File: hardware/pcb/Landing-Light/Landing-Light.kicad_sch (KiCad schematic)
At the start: 26 parts, among them J1 Conn_01x04, SW1 SW_SPST, SW2 SW_SP3T, U1 BQ25172DSGR, U2 TPS61022

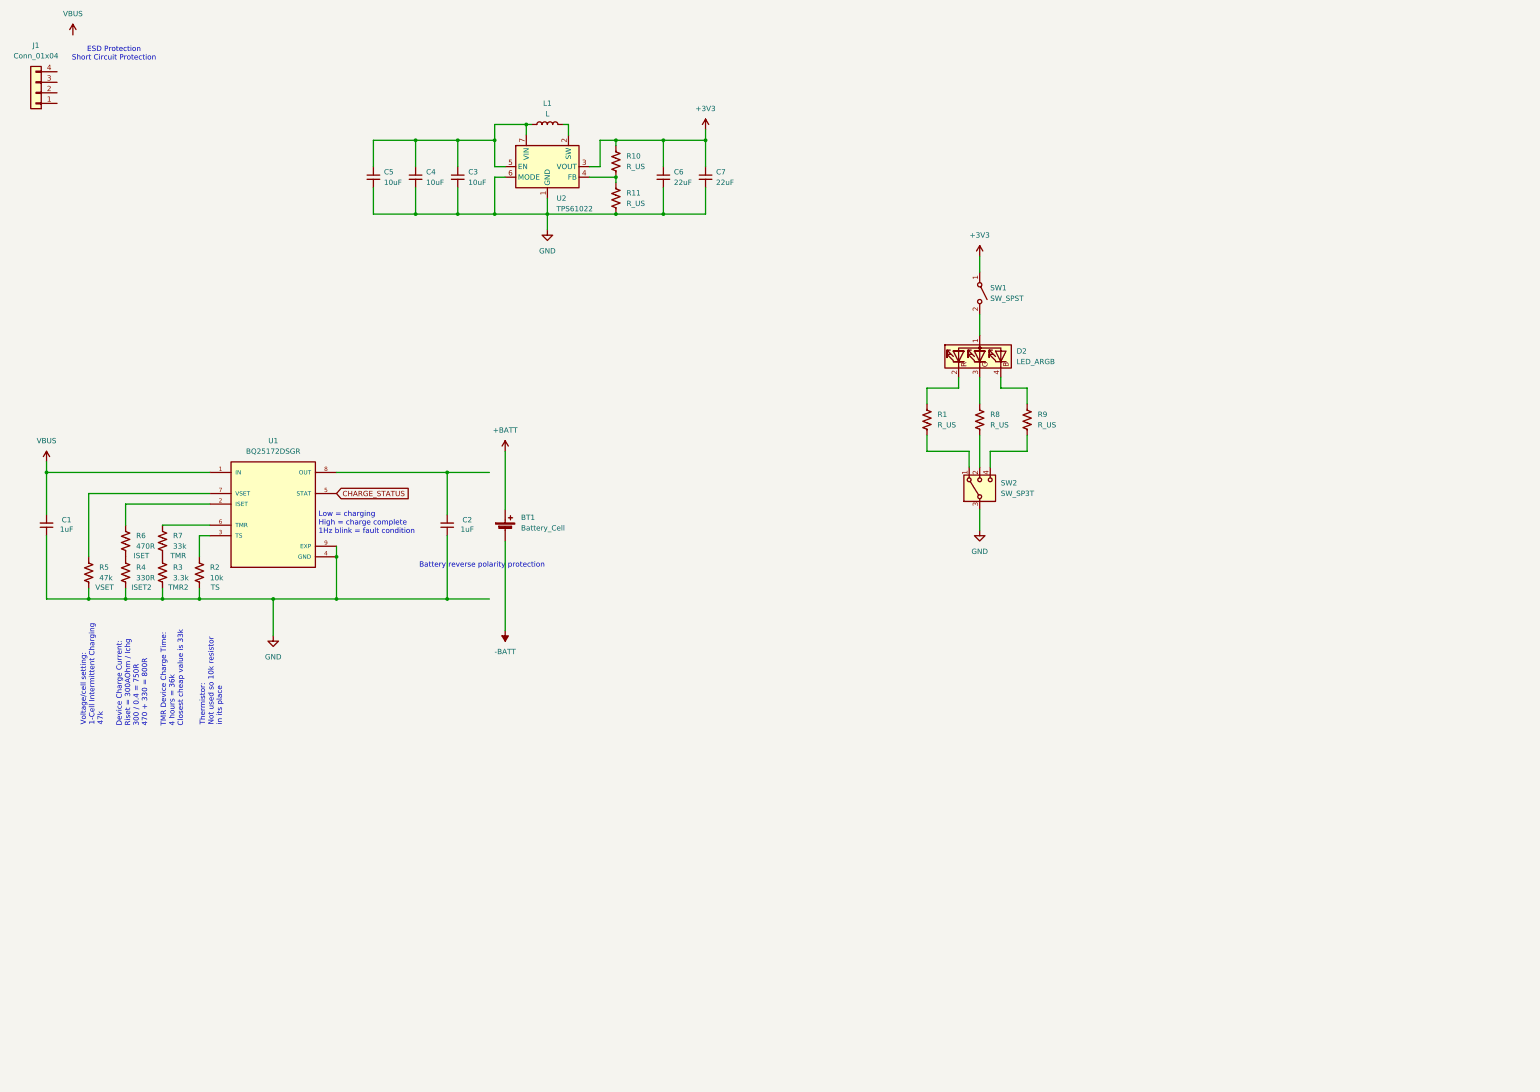
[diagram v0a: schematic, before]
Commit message: Footprints complete
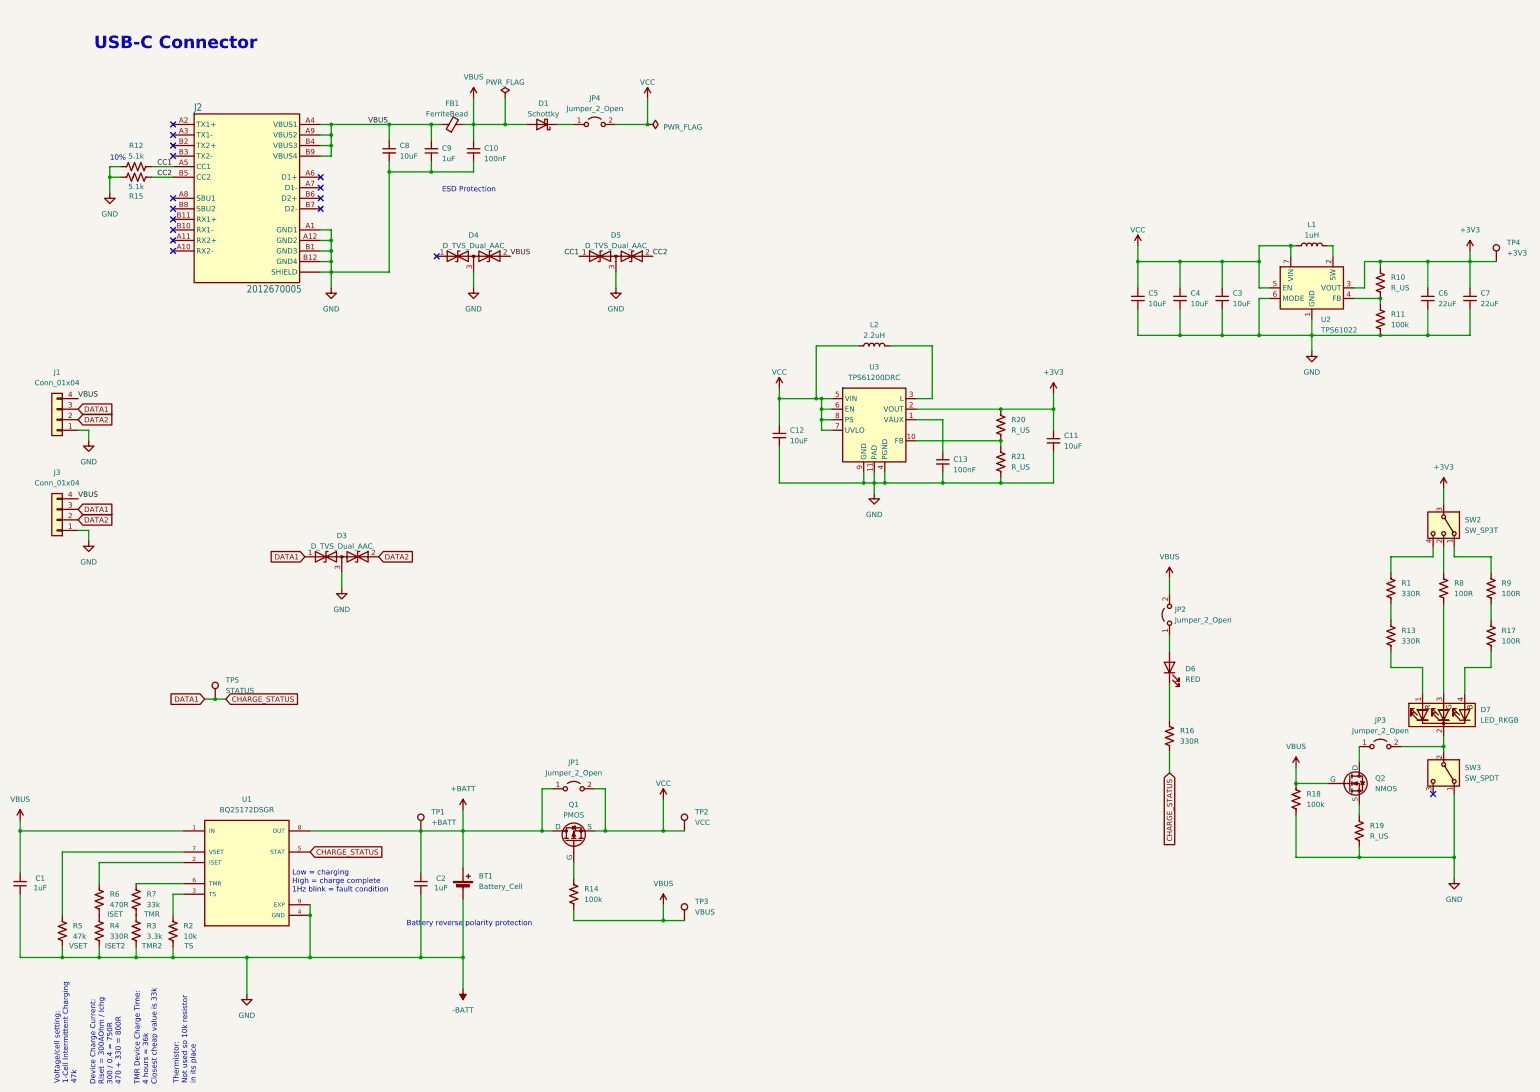
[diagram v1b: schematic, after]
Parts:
- removed D2: LED_ARGB, LED_THT:LED_D5.0mm-4_RGB_Staggered_Pins, symbol Device:LED_ARGB
- removed SW1: SW_SPST, Button_Switch_SMD:SW_SPDT_PCM12, symbol Switch:SW_SPST
- added C10, C13: 100nF, Capacitor_SMD:C_0402_1005Metric, symbol Device:C_Small
- added C11, C12, C8: 10uF, Capacitor_SMD:C_0603_1608Metric, symbol Device:C_Small
- added C9: 1uF, Capacitor_SMD:C_0402_1005Metric, symbol Device:C_Small
- added D1: Schottky, Diode_SMD:D_SMA, symbol Device:D_Schottky
- added D3, D4, D5: D_TVS_Dual_AAC, Package_TO_SOT_SMD:SOT-23, symbol Device:D_TVS_Dual_AAC
- added D6: RED, LED_SMD:LED_0805_2012Metric, symbol Device:LED
- added D7: LED_RKGB, LED_THT:LED_D5.0mm-4_RGB, symbol Device:LED_RKGB
- added FB1: FerriteBead, Diode_SMD:D_0805_2012Metric, symbol Device:FerriteBead_Small
- added J2: 2012670005, Landing-Light:MOLEX_2012670005, symbol ESP32_Dev_Board-eagle-import:2012670005
- added J3: Conn_01x04, Connector_PinHeader_2.54mm:PinHeader_1x04_P2.54mm_Vertical, symbol Connector_Generic:Conn_01x04
- added JP1, JP2, JP3, JP4: Jumper_2_Open, Jumper:SolderJumper-2_P1.3mm_Open_Pad1.0x1.5mm, symbol Jumper:Jumper_2_Open
- added L2: 2.2uH, Inductor_SMD:L_Sunlord_SWPA3015S, symbol Device:L
- added Q1: PMOS, Package_TO_SOT_SMD:SOT-23, symbol Simulation_SPICE:PMOS
- added Q2: NMOS, Package_TO_SOT_SMD:SOT-23-3, symbol Simulation_SPICE:NMOS
- added R12, R15: 5.1k, Resistor_SMD:R_0603_1608Metric, symbol Device:R_US
- added R13, R16: 330R, Resistor_SMD:R_0402_1005Metric, symbol Device:R_US
- added R14, R18: 100k, Resistor_SMD:R_0603_1608Metric, symbol Device:R_US
- added R17: 100R, Resistor_SMD:R_0402_1005Metric, symbol Device:R_US
- added R19, R20, R21: R_US, Resistor_SMD:R_0603_1608Metric, symbol Device:R_US
- added SW3: SW_SPDT, Landing-Light:SSSS810201, symbol Switch:SW_SPDT
- added TP1: +BATT, TestPoint:TestPoint_Pad_D1.0mm, symbol Connector:TestPoint
- added TP2: VCC, TestPoint:TestPoint_Pad_D1.0mm, symbol Connector:TestPoint
- added TP3: VBUS, TestPoint:TestPoint_Pad_D1.0mm, symbol Connector:TestPoint
- added TP4: +3V3, TestPoint:TestPoint_Pad_D1.0mm, symbol Connector:TestPoint
- added TP5: STATUS, TestPoint:TestPoint_Pad_D1.0mm, symbol Connector:TestPoint
- added U3: TPS61200DRC, Package_SON:Texas_S-PVSON-N10_ThermalVias, symbol Regulator_Switching:TPS61200DRC
- J1: footprint (none) -> Landing-Light:70AAJ-4-F1G
- L1: value L -> 1uH
- R1: value R_US -> 330R; LCSC (none) -> C25104
- R11: value R_US -> 100k; footprint Resistor_SMD:R_0402_1005Metric -> Resistor_SMD:R_0603_1608Metric; LCSC (none) -> C25803
- R2, R3, R4, R5, R6, R7: footprint Capacitor_SMD:C_0402_1005Metric -> Resistor_SMD:R_0402_1005Metric
- R8, R9: value R_US -> 100R; LCSC (none) -> C25076
- SW2: footprint Button_Switch_SMD:SW_SPDT_PCM12 -> Landing-Light:SSSS812201; LCSC (none) -> C160878; now left out of the parts list
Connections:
- net +3V3: now also SW2.3, C11.1, R20.1, TP4.1, U3.2 (VOUT)
- net +BATT: now also C2.2, U1.8 (OUT), JP1.1 (A), Q1.3 (D), TP1.1
- net -BATT: now also C1.1, C2.1, C3.2, C4.2, C5.2, C6.2, C7.2, J1.1 (Pin_1), R11.2, R2.2, R3.2, R4.2, R5.2, U1.4 (GND), U1.9 (EXP), U2.1 (GND), U2.6 (MODE), C10.2, C11.2, C12.2, C13.2, C8.2, C9.1, D3.3 (common), D4.3 (common), D5.3 (common), J2.A1 (GND1), J2.A12 (GND2), J2.B1 (GND3), J2.B12 (GND4), J2.S1 (SHIELD), J2.S2 (SHIELD), J2.S3 (SHIELD), J2.S4 (SHIELD), J3.1 (Pin_1), R12.1, R15.2, R18.2, R19.2, R21.2, SW3.1 (A), U3.11 (PAD), U3.4 (PGND), U3.9 (GND)
- net CHARGE_STATUS: now also J1.3 (Pin_3), D3.1 (A1), J3.3 (Pin_3), R16.2, TP5.1
- net VBUS: now also J1.4 (Pin_4), C10.1, C8.1, C9.2, D1.2 (A), D4.2 (A2), FB1.1, FB1.2, J2.A4 (VBUS1), J2.A9 (VBUS2), J2.B4 (VBUS3), J2.B9 (VBUS4), J3.4 (Pin_4), JP2.2 (B), Q2.2 (G), R14.2, R18.1, TP3.1
- net VCC: now reaches C3.1, C4.1, C5.1, L1.1, U2.5 (EN), U2.7 (VIN)
- net VCC: now also C12.1, JP1.2 (B), JP4.2 (B), L2.1, Q1.2 (S), TP2.1, U3.5 (VIN), U3.6 (EN), U3.7 (UVLO), U3.8 (PS)
- net at R1.1: now also SW2.4
- net at R8.1: now also SW2.2
- net at R9.1: now also SW2.1
- net at R1.2: now also R13.1; no longer SW2.1
- net at R8.2: now also D7.3 (GA); no longer SW2.2
- net at R9.2: now also R17.1; no longer SW2.4
- net DATA2: now reaches J1.2 (Pin_2)
- net DATA2: now also D3.2 (A2), J3.2 (Pin_2)
- removed net GND: C1.1, C2.1, C3.2, C4.2, C5.2, C6.2, C7.2, R11.2, R2.2, R3.2, R4.2, R5.2, SW2.3, U1.4 (GND), U1.9 (EXP), U2.1 (GND), U2.6 (MODE)
- new net: D6.1 (K), R16.1
- new net: D6.2 (A), JP2.1 (A)
- new net: D7.4 (BA), R17.2
- new net: L2.2, U3.3 (L)
- new net: Q2.3 (S), R19.1
- new net: Q1.1 (G), R14.1
- new net: D7.2 (K), JP3.2 (B), SW3.2 (B)
- new net: D1.1 (K), JP4.1 (A)
- new net: C13.1, U3.1 (VAUX)
- new net: JP3.1 (A), Q2.1 (D)
- new net: R20.2, R21.1, U3.10 (FB)
- new net: D7.1 (RA), R13.2
- new net CC1: D5.1 (A1), J2.A5 (CC1), R12.2
- new net CC2: D5.2 (A2), J2.B5 (CC2), R15.1
- no-connect marks 0 -> 16
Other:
- note added: "10%"
- note added: "ESD Protection"
- note added: "USB-C Connector"
- note removed: "ESD Protection Short Circuit Protection"
- moved on the sheet: BT1, C1, C2, C3, C4, C5, C6, C7, J1, L1, R10, R2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

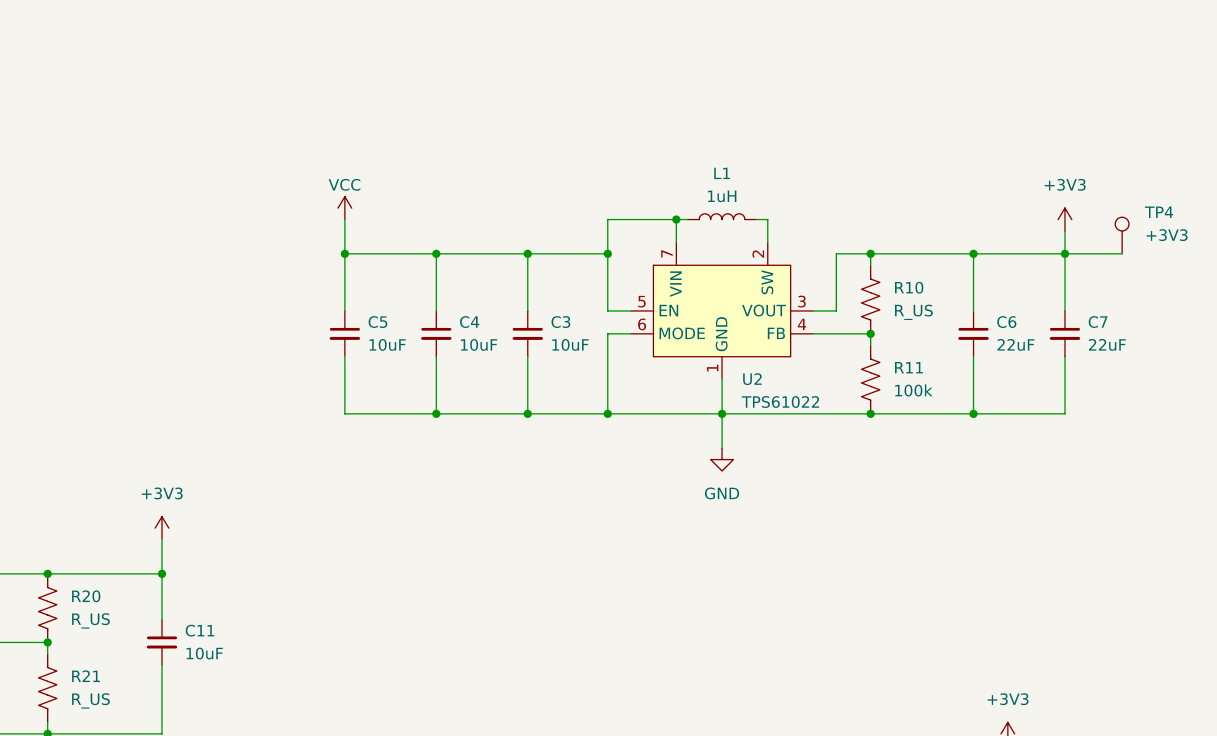
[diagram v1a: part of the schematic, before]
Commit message: Removing old regulator
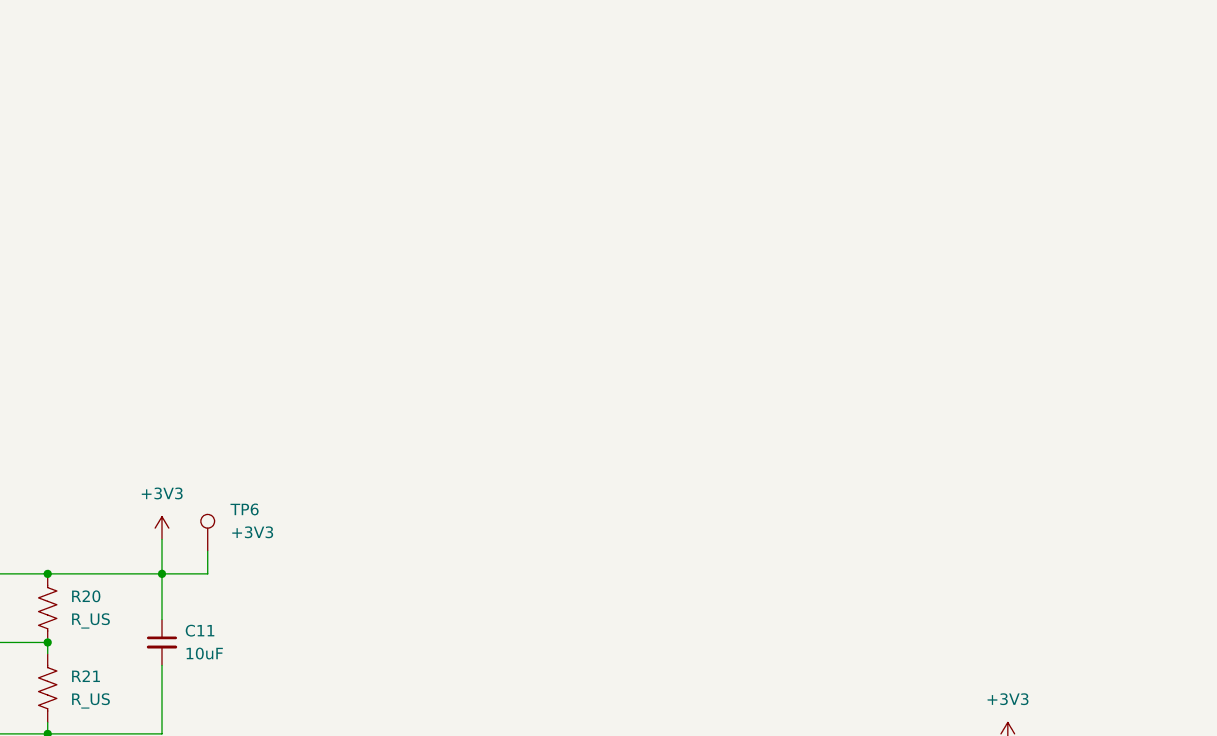
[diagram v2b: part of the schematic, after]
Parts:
- removed C3, C4, C5: 10uF, Capacitor_SMD:C_0603_1608Metric, symbol Device:C_Small
- removed C6, C7: 22uF, Capacitor_SMD:C_0805_2012Metric, symbol Device:C_Small
- removed L1: 1uH, Inductor_SMD:L_Sunlord_SWPA4030S, symbol Device:L
- removed R10: R_US, Resistor_SMD:R_0603_1608Metric, symbol Device:R_US
- removed R11: 100k, Resistor_SMD:R_0603_1608Metric, symbol Device:R_US
- removed TP4: +3V3, TestPoint:TestPoint_Pad_D1.0mm, symbol Connector:TestPoint
- removed U2: TPS61022, Package_DFN_QFN:Texas_RWU0007A_VQFN-7_2x2mm_P0.5mm, symbol Converter_DCDC:TPS61022
- added TP6: +3V3, TestPoint:TestPoint_Pad_D1.0mm, symbol Connector:TestPoint
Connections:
- net +3V3: now also TP6.1

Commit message: TVS Diode LCSC Number
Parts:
- removed D5: D_TVS_Dual_AAC, Package_TO_SOT_SMD:SOT-23, symbol Device:D_TVS_Dual_AAC
- added D2: D_TVS_Dual_AAC, Package_TO_SOT_SMD:SOT-23, symbol Device:D_TVS_Dual_AAC
- D3, D4: LCSC (none) -> C32677
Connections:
- net -BATT: now also D2.3 (common)
- net CC1: now also D2.1 (A1)
- net CC2: now also D2.2 (A2)
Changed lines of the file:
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@@
 	)
 	(symbol
+		(lib_id "Device:D_TVS_Dual_AAC")
+		(at 165.1 78.74 0)
+		(unit 1)
+		(exclude_from_sim no)
+		(in_bom no)
+		(on_board yes)
+		(dnp no)
+		(fields_autoplaced yes)
+		(property "Reference" "D2"
+			(at 165.1 73.66 0)
+			(effects
+				(font
+					(size 1.27 1.27)
+				)
+			)
+		)
+		(property "Value" "D_TVS_Dual_AAC"
+			(at 165.1 76.2 0)
+			(effects
+				(font
+					(size 1.27 1.27)
+				)
+			)
+		)
+		(property "Footprint" "Package_TO_SOT_SMD:SOT-23"
+			(at 161.29 78.74 0)
+			(effects
+				(font
+					(size 1.27 1.27)
+				)
+				(hide yes)
+			)
+		)
+		(property "Datasheet" "~"
+			(at 161.29 78.74 0)
+			(effects
+				(font
+					(size 1.27 1.27)
+				)
+				(hide yes)
+			)
+		)
+		(property "Description" "Bidirectional dual transient-voltage-suppression diode, center on pin 3"
+			(at 165.1 78.74 0)
+			(effects
+				(font
+					(size 1.27 1.27)
+				)
+				(hide yes)
+			)
+		)
+		(property "LCSC" "C32677"
+			(at 165.1 78.74 0)
+			(effects
+				(font
+					(size 1.27 1.27)
+				)
+				(hide yes)
+			)
+		)
+		(pin "3"
+		)
+		(pin "2"
+		)
+		(pin "1"
+		)
+		(instances
+			(project "Landing-Light"
+				(path "/f89d3217-1b1a-43a4-8c74-9ff6f0eaa6ee"
+					(reference "D2")
+					(unit 1)
+				)
+			)
+		)
+	)
+	(symbol
 		(lib_id "Device:R_US")
 		(at 344.17 217.17 0)
@@
 	)
 	(symbol
-		(lib_id "Device:D_TVS_Dual_AAC")
-		(at 99.06 151.13 0)
-		(unit 1)
-		(exclude_from_sim no)
-		(in_bom no)
-		(on_board yes)
-		(dnp no)
-		(fields_autoplaced yes)
-		(property "Reference" "D3"
-			(at 99.06 146.05 0)
-			(effects
-				(font
-					(size 1.27 1.27)
-				)
-			)
-		)
-		(property "Value" "D_TVS_Dual_AAC"
-			(at 99.06 148.59 0)
-			(effects
-				(font
-					(size 1.27 1.27)
-				)
-			)
-		)
-		(property "Footprint" "Package_TO_SOT_SMD:SOT-23"
-			(at 95.25 151.13 0)
-			(effects
-				(font
-					(size 1.27 1.27)
-				)
-				(hide yes)
-			)
-		)
-		(property "Datasheet" "~"
-			(at 95.25 151.13 0)
-			(effects
-				(font
-					(size 1.27 1.27)
-				)
-				(hide yes)
-			)
-		)
-		(property "Description" "Bidirectional dual transient-voltage-suppression diode, center on pin 3"
-			(at 99.06 151.13 0)
-			(effects
-				(font
-					(size 1.27 1.27)
-				)
-				(hide yes)
-			)
-		)
-		(pin "3"
-		)
-		(pin "2"
-		)
-		(pin "1"
-		)
-		(instances
-			(project "Landing-Light"
-				(path "/f89d3217-1b1a-43a4-8c74-9ff6f0eaa6ee"
-					(reference "D3")
-					(unit 1)
-				)
-			)
-		)
-	)
-	(symbol
 		(lib_id "Device:R_US")
 		(at 257.81 128.27 0)
@@
 	)
 	(symbol
-		(lib_id "Device:D_TVS_Dual_AAC")
-		(at 165.1 78.74 0)
-		(unit 1)
-		(exclude_from_sim no)
-		(in_bom no)
-		(on_board yes)
-		(dnp no)
-		(fields_autoplaced yes)
-		(property "Reference" "D5"
-			(at 165.1 73.66 0)
-			(effects
-				(font
-					(size 1.27 1.27)
-				)
-			)
-		)
-		(property "Value" "D_TVS_Dual_AAC"
-			(at 165.1 76.2 0)
-			(effects
-				(font
-					(size 1.27 1.27)
-				)
-			)
-		)
-		(property "Footprint" "Package_TO_SOT_SMD:SOT-23"
-			(at 161.29 78.74 0)
-			(effects
-				(font
-					(size 1.27 1.27)
-				)
-				(hide yes)
-			)
-		)
-		(property "Datasheet" "~"
-			(at 161.29 78.74 0)
-			(effects
-				(font
-					(size 1.27 1.27)
-				)
-				(hide yes)
-			)
-		)
-		(property "Description" "Bidirectional dual transient-voltage-suppression diode, center on pin 3"
-			(at 165.1 78.74 0)
-			(effects
-				(font
-					(size 1.27 1.27)
-				)
-				(hide yes)
-			)
-		)
-		(pin "3"
-		)
-		(pin "2"
-		)
-		(pin "1"
-		)
-		(instances
-			(project "Landing-Light"
-				(path "/f89d3217-1b1a-43a4-8c74-9ff6f0eaa6ee"
-					(reference "D5")
-					(unit 1)
-				)
-			)
-		)
-	)
-	(symbol
 		(lib_id "Device:R_US")
 		(at 154.94 232.41 0)
@@
 	)
 	(symbol
+		(lib_id "Device:D_TVS_Dual_AAC")
+		(at 99.06 151.13 0)
+		(unit 1)
+		(exclude_from_sim no)
+		(in_bom no)
+		(on_board yes)
+		(dnp no)
+		(fields_autoplaced yes)
+		(property "Reference" "D3"
+			(at 99.06 146.05 0)
+			(effects
+				(font
+					(size 1.27 1.27)
+				)
+			)
+		)
+		(property "Value" "D_TVS_Dual_AAC"
+			(at 99.06 148.59 0)
+			(effects
+				(font
+					(size 1.27 1.27)
+				)
+			)
+		)
+		(property "Footprint" "Package_TO_SOT_SMD:SOT-23"
+			(at 95.25 151.13 0)
+			(effects
+				(font
+					(size 1.27 1.27)
+				)
+				(hide yes)
+			)
+		)
+		(property "Datasheet" "~"
+			(at 95.25 151.13 0)
+			(effects
+				(font
+					(size 1.27 1.27)
+				)
+				(hide yes)
+			)
+		)
+		(property "Description" "Bidirectional dual transient-voltage-suppression diode, center on pin 3"
+			(at 99.06 151.13 0)
+			(effects
+				(font
+					(size 1.27 1.27)
+				)
+				(hide yes)
+			)
+		)
+		(property "LCSC" "C32677"
+			(at 99.06 151.13 0)
+			(effects
+				(font
+					(size 1.27 1.27)
+				)
+				(hide yes)
+			)
+		)
+		(pin "3"
+		)
+		(pin "2"
+		)
+		(pin "1"
+		)
+		(instances
+			(project "Landing-Light"
+				(path "/f89d3217-1b1a-43a4-8c74-9ff6f0eaa6ee"
+					(reference "D3")
+					(unit 1)
+				)
+			)
+		)
+	)
+	(symbol
 		(lib_id "power:VBUS")
 		(at 176.53 234.95 0)
@@
 			(at 130.81 78.74 0)
 			(effects
+				(font
+					(size 1.27 1.27)
+				)
+				(hide yes)
+			)
+		)
+		(property "LCSC" "C32677"
+			(at 130.81 78.74 0)
+			(effects
